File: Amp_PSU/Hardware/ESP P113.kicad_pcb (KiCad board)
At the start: 2 copper layers, 100.3 x 72.4 mm, 61 parts, among them J1 L_In, J2 R_In, J3 L_Out, J4 R_Out, J5 AC_In, Q1 MJE15032, Q2 MJE15033, Q3 MJE15032, Q4 MJE15033, U1 LM4562

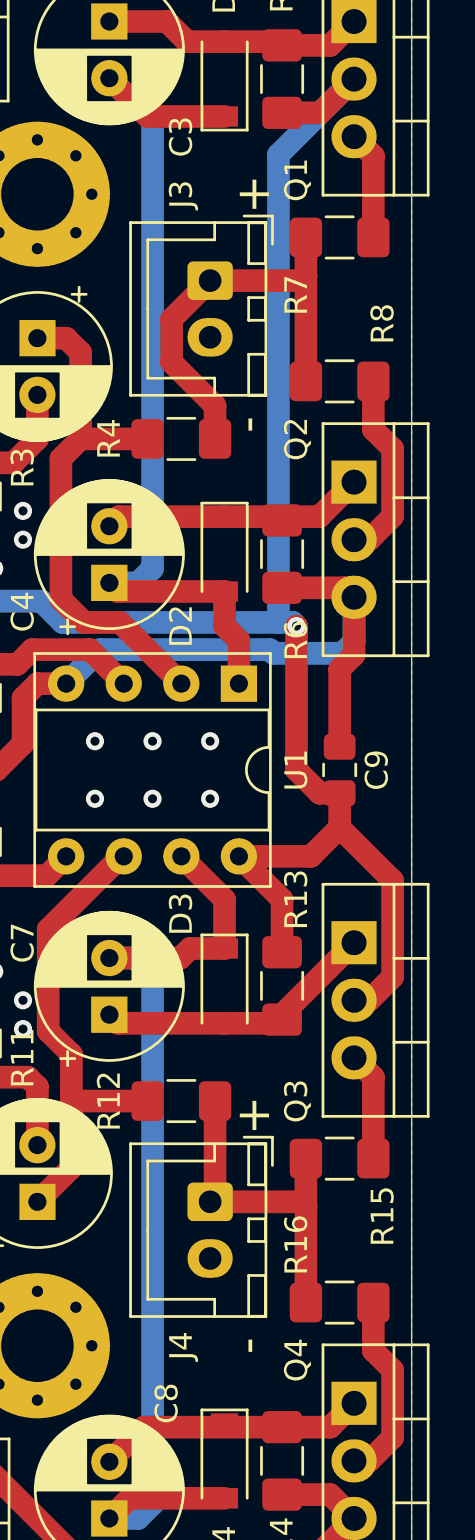
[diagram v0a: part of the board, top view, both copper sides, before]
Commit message: Slightly moved position of output resistors.
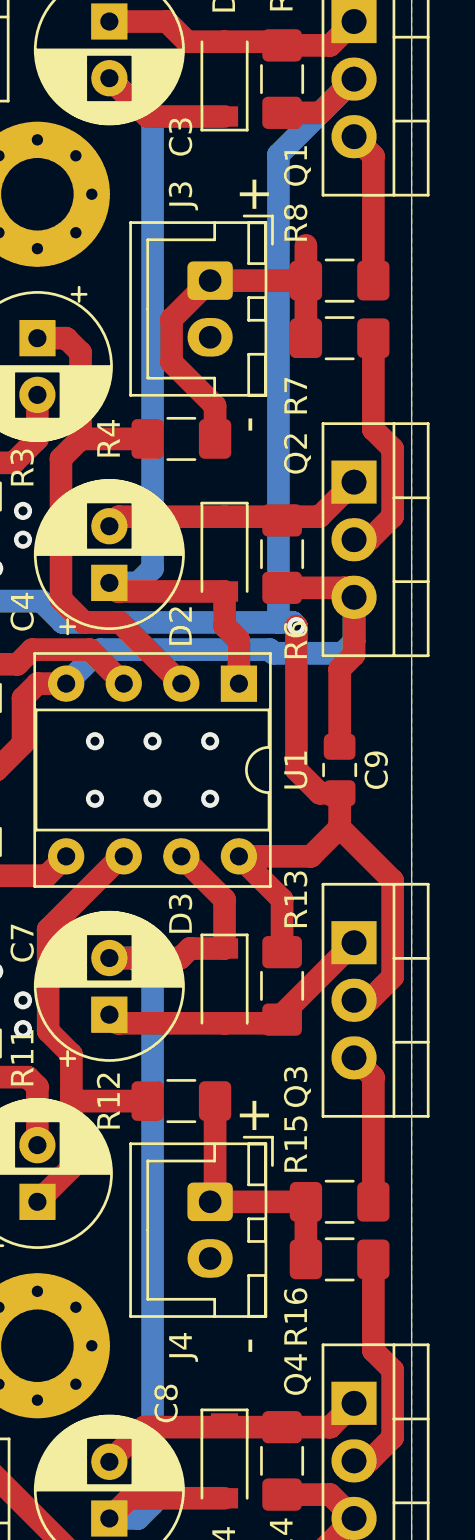
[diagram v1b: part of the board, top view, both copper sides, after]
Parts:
- moved R15 1.91 mm to (156.8, 81.3)
- moved R16 1.91 mm to (156.8, 83.8)
- moved R7 1.91 mm to (156.8, 40.6)
- moved R8 1.91 mm to (156.8, 43.2)
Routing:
- net R_Out: track 15.2 -> 11.1 mm
- net L_Out: track 18.8 -> 16.7 mm
- net Net-(Q4-Pad2): track 8.43 -> 10.3 mm
- net Net-(Q3-Pad3): track 4.80 -> 6.70 mm
- net Net-(Q2-Pad2): track 8.43 -> 10.3 mm
- net Net-(Q1-Pad3): track 4.80 -> 6.70 mm

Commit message: Revert "Slightly moved position of output resistors."
This reverts commit 2c67a83915dd1cff94a26fcd4de2be662b6489d6.
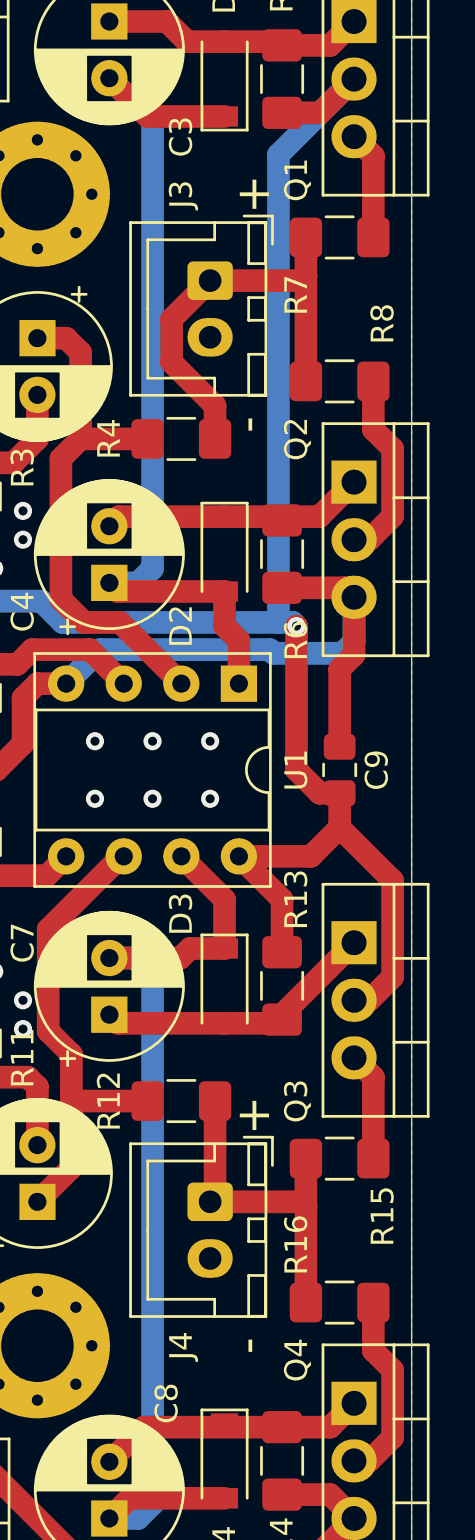
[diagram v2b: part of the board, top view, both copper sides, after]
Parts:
- moved R15 1.91 mm to (156.8, 79.4)
- moved R16 1.91 mm to (156.8, 85.7)
- moved R7 1.91 mm to (156.8, 38.7)
- moved R8 1.91 mm to (156.8, 45.1)
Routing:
- net R_Out: track 11.1 -> 15.2 mm
- net L_Out: track 16.7 -> 18.8 mm
- net Net-(Q4-Pad2): track 10.3 -> 8.43 mm
- net Net-(Q3-Pad3): track 6.70 -> 4.80 mm
- net Net-(Q2-Pad2): track 10.3 -> 8.43 mm
- net Net-(Q1-Pad3): track 6.70 -> 4.80 mm
